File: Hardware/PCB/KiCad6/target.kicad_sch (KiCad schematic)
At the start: 48 parts, among them J2 SW-5V, J3 SW-1, J4 SW-3.3V, J5 SW-2, J6 EXT_LED, J7 Conn_IN, J8 Conn_OUT, Q1 BSS138, Q2 BSS138, Q3 BSS138, Q4 BSS138, U1 ESP32-WROOM-32D, U2 TSOP312xx

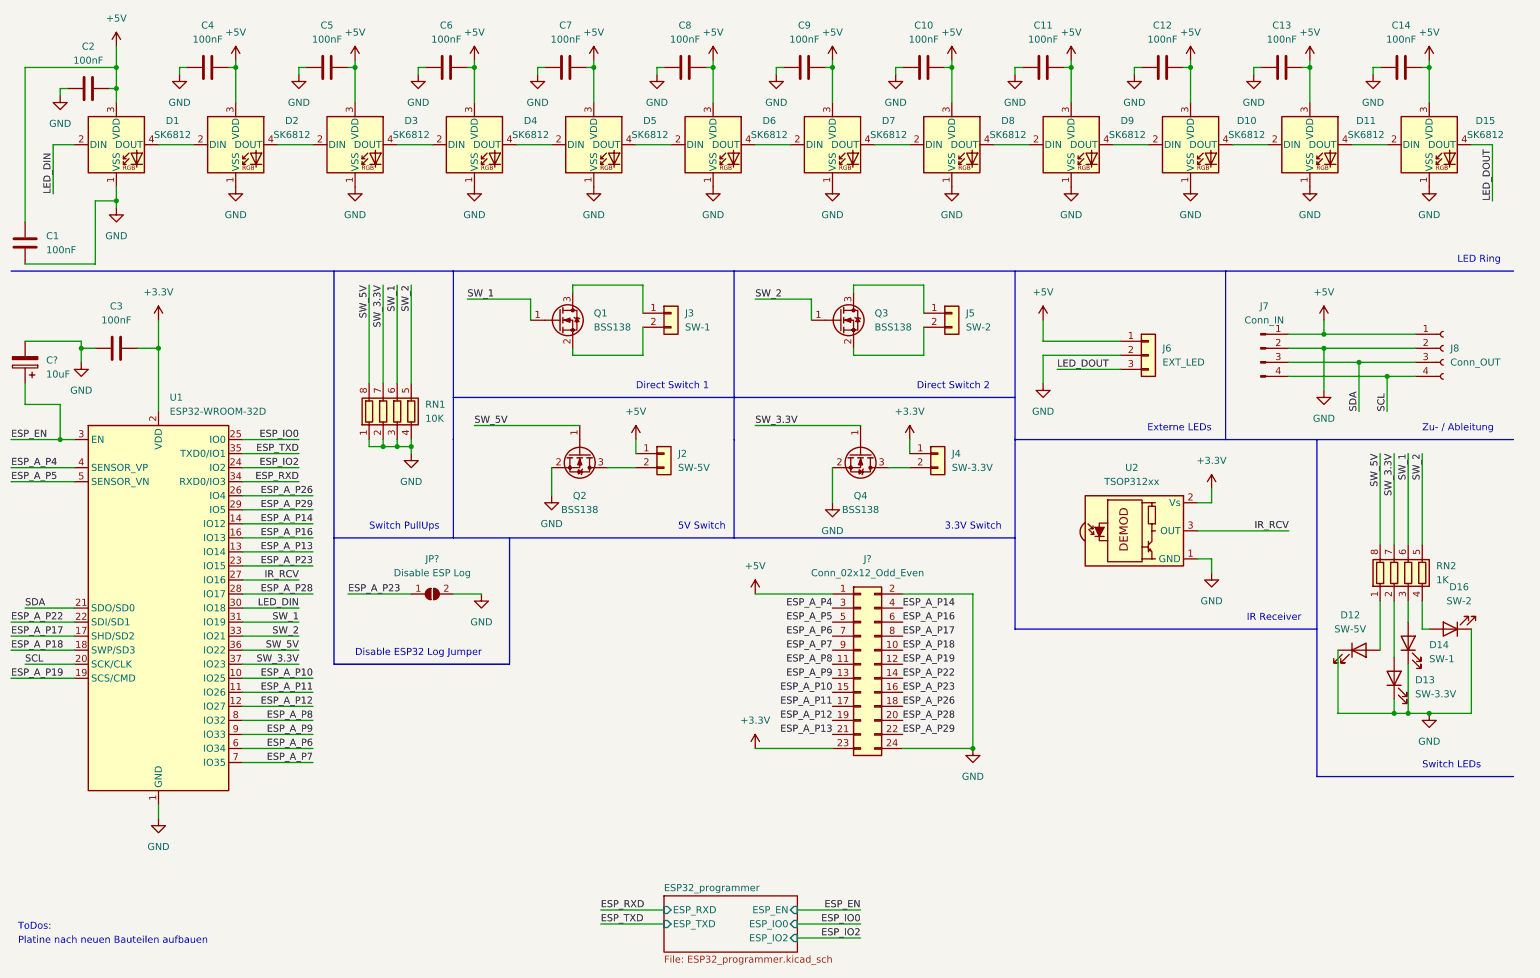
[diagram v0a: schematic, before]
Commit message: PCB Update from current schema
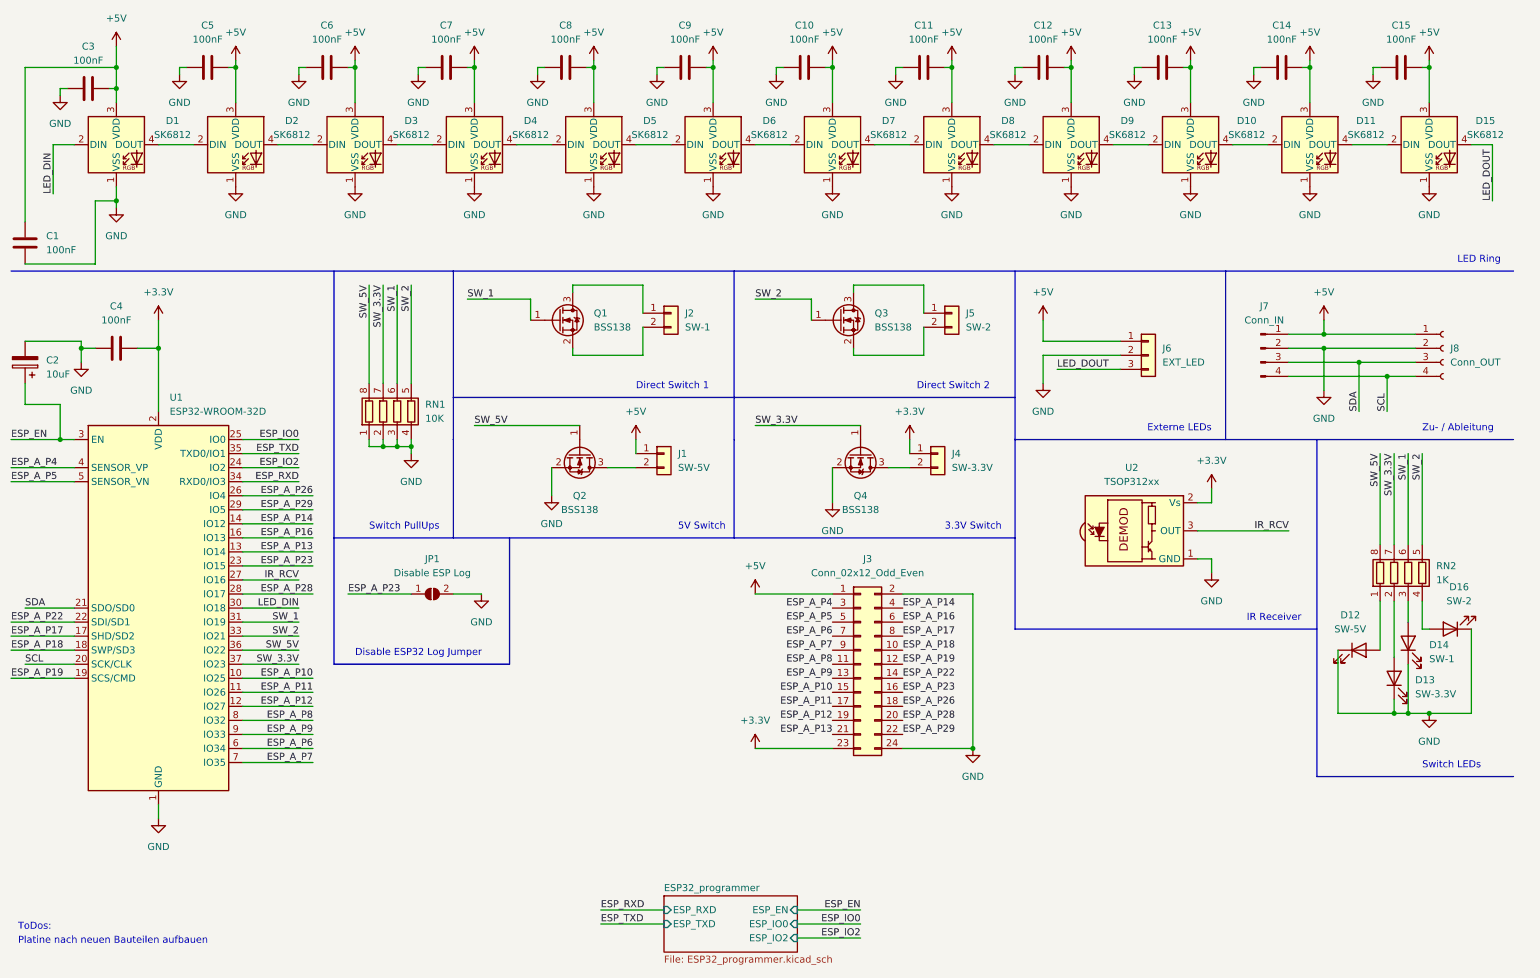
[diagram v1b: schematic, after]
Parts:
- C2: renamed from C?; footprint (none) -> Capacitor_Tantalum_SMD:CP_EIA-2012-12_Kemet-R_Pad1.30x1.05mm_HandSolder; LCSC (none) -> C2976905
- D1, D10, D11, D15, D2, D3, D4, D5, D6, D7, D8, D9: LCSC (none) -> C5160656
- J3: renamed from J?; footprint (none) -> Connector_PinHeader_2.54mm:PinHeader_2x12_P2.54mm_Vertical; LCSC (none) -> C62744
- JP1: renamed from JP?; footprint (none) -> Jumper:SolderJumper-2_P1.3mm_Open_RoundedPad1.0x1.5mm
- renumbered C9 to C10, C10 to C11, C11 to C12, C12 to C13, C13 to C14, C14 to C15, C2 to C3, C3 to C4, C4 to C5, C5 to C6, C6 to C7, C7 to C8, C8 to C9, J2 to J1, J3 to J2
